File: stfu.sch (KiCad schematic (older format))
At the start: 136 parts, among them K1 FTDI, K2 ISP, K3 I2C, K4 SERVO, K5 V_SEL, P1 CONN_1, P2 CONN_1, Q1 PNP, SW1 RST, SW2 RST, SW3 SW_MODE, SW4 SW_INC, SW5 SW_DEC, SW6 SW_ENT, U1 ATMEGA328-P, U2 HEF4051B, U3 ULN2803, U4 7809, U5 7805, X1 16MHz

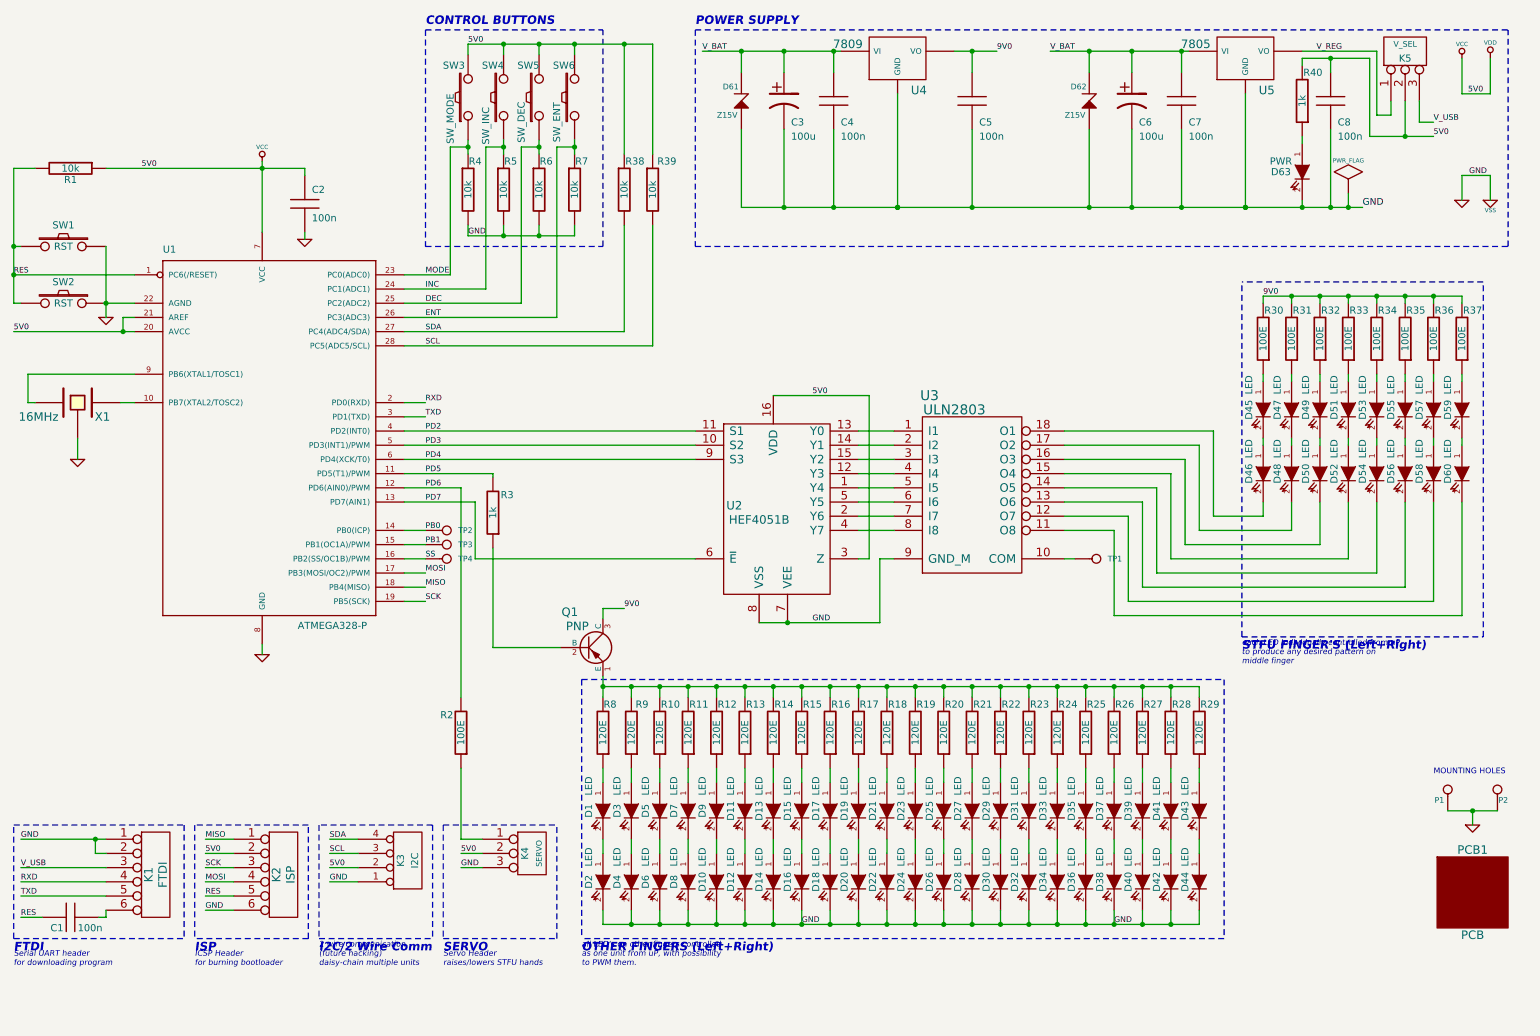
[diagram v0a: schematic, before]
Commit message: added the second Hand
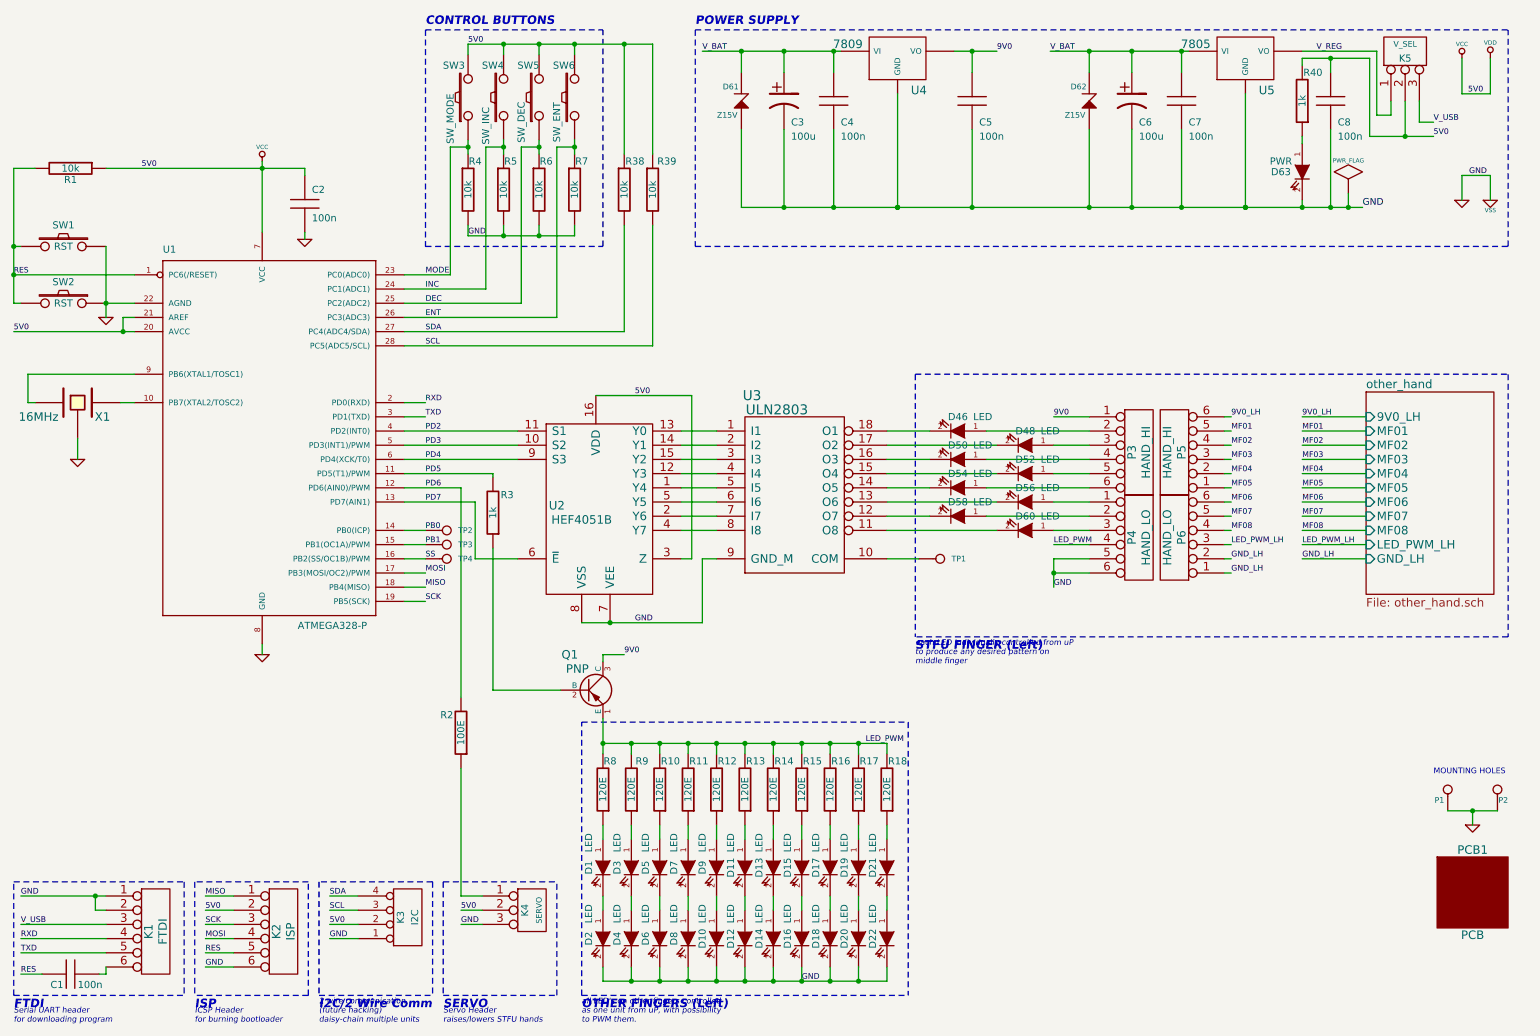
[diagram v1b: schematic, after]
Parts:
- removed D23, D24, D25, D26, D27, D28, D29, D30, D31, D32, D33, D34, D35, D36, D37, D38, D39, D40, D41, D42, D43, D44, D45, D47, D49, D51, D53, D55, D57, D59: LED, symbol LED
- removed R19, R20, R21, R22, R23, R24, R25, R26, R27, R28, R29: 120E, r_0805, symbol R
- removed R30, R31, R32, R33, R34, R35, R36, R37: 100E, r_0805, symbol R
- added P3, P5: HAND_HI, symbol CONN_6
- added P4, P6: HAND_LO, symbol CONN_6
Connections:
- net 9V0: now also P3.1
- net GND: now also P4.5, P4.6
- net LED_PWM: now reaches Q1.1 (E), R10.2, R11.2, R12.2, R13.2, R14.2, R15.2, R16.2, R17.2, R18.2, R8.2, R9.2
- net LED_PWM: now also P4.4
- net at D46.1 (A): now also P3.2
- net at D48.1 (A): now also P3.3
- net at D50.1 (A): now also P3.4
- net at D52.1 (A): now also P3.5
- net at D54.1 (A): now also P3.6
- net at D56.1 (A): now also P4.1
- net at D58.1 (A): now also P4.2
- net at D60.1 (A): now also P4.3
- new net 9V0_LH: P5.6
- new net GND_LH: P6.1, P6.2
- new net LED_PWM_LH: P6.3
- new net MF01: P5.5
- new net MF02: P5.4
- new net MF03: P5.3
- new net MF04: P5.2
- new net MF05: P5.1
- new net MF06: P6.6
- new net MF07: P6.5
- new net MF08: P6.4
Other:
- note added: "OTHER FINGERS (Left)"
- note added: "STFU FINGER (Left)"
- note removed: "OTHER FINGERS (Left+Right)"
- note removed: "STFU FINGER'S (Left+Right)"
- moved on the sheet: C1, D1, D10, D11, D12, D13, D14, D15, D16, D17, D18, D19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

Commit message: preliminary board layout
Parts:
- added P7: BATT_12V, symbol CONN_2
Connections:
- net GND: now also P7.1 (P1)
- net V_BAT: now also P7.2 (PM)
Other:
- moved on the sheet: C3, C4, C5, C6, D61, D62, U4
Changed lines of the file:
@@
-EESchema Schematic File Version 2  date 7/5/2012 5:41:43 PM
+EESchema Schematic File Version 2  date Monday 09 July 2012 12:59:22 AM IST
 LIBS:stfu
 LIBS:power
@@
 Sheet 1 2
 Title "STFU - a warning for incessant Noise polluters"
-Date "5 jul 2012"
+Date "8 jul 2012"
 Rev "A"
 Comp "anool.m@gmail.com"
@@
 $EndDescr
 Wire Notes Line
+	5600 2150 11125 2150
+Wire Notes Line
+	5600 2150 5600 625
+Wire Wire Line
+	6150 1375 6150 775
+Wire Wire Line
+	6150 1375 6100 1375
+Wire Notes Line
 	6950 3050 6950 4900
 Wire Notes Line
@@
 Wire Wire Line
 	6750 7325 4750 7325
-Connection ~ 8175 1875
-Wire Wire Line
-	8175 1875 8175 1325
+Connection ~ 8375 1875
+Wire Wire Line
+	8375 1875 8375 1325
 Wire Notes Line
 	3500 625  4750 625
@@
 Wire Notes Line
 	4750 2150 4750 625
-Wire Notes Line
-	5400 625  5400 2150
 Wire Wire Line
 	4900 5025 4750 5025
 Wire Wire Line
 	4750 5025 4750 5075
-Connection ~ 7350 775
-Wire Wire Line
-	7350 925  7350 775
-Connection ~ 5725 775
-Wire Wire Line
-	5725 925  5725 775
-Connection ~ 6825 1875
-Connection ~ 6375 775
-Connection ~ 6375 1875
-Wire Wire Line
-	6375 1875 6375 1325
-Connection ~ 6825 1875
-Wire Wire Line
-	6025 1325 6025 1875
-Wire Wire Line
-	6025 775  6025 925
-Wire Wire Line
-	6825 1875 6825 1075
-Wire Wire Line
-	6375 775  6375 925
-Connection ~ 6025 775
-Wire Wire Line
-	6425 775  5450 775
-Wire Wire Line
-	5725 1325 5725 1875
-Connection ~ 6025 1875
+Connection ~ 7750 775
+Wire Wire Line
+	7750 925  7750 775
+Connection ~ 6325 775
+Wire Wire Line
+	6325 775  6325 925
+Connection ~ 7275 1875
+Connection ~ 6775 775
+Connection ~ 6775 1875
+Wire Wire Line
+	6775 1875 6775 1325
+Connection ~ 7275 1875
+Wire Wire Line
+	6525 1875 6525 1325
+Wire Wire Line
+	6525 775  6525 925
+Wire Wire Line
+	7275 1875 7275 1075
+Wire Wire Line
+	6775 925  6775 775
+Connection ~ 6525 775
+Wire Wire Line
+	6150 775  6875 775
+Wire Wire Line
+	6325 1325 6325 1875
+Connection ~ 6525 1875
 Wire Wire Line
 	6750 4150 7525 4150
@@
 Wire Wire Line
 	650  2150 600  2150
-Connection ~ 8475 1875
-Wire Wire Line
-	5725 1875 10100 1875
+Connection ~ 8575 1875
 Connection ~ 10875 6125
 Wire Wire Line
@@
 	1950 7125 2150 7125
 Wire Wire Line
-	8875 775  7900 775
-Connection ~ 8475 775
+	8875 775  8175 775
+Connection ~ 8575 775
 Connection ~ 9875 825
 Wire Wire Line
 	9875 925  9875 825
 Wire Wire Line
-	8825 925  8825 775
+	8825 775  8825 925
 Wire Wire Line
 	9675 1875 9675 1825
@@
 	9275 1875 9275 1075
 Wire Wire Line
-	8475 775  8475 925
+	8575 775  8575 925
 Connection ~ 9675 1875
 Wire Wire Line
-	8475 1875 8475 1325
+	8575 1875 8575 1325
 Connection ~ 9275 1875
 Wire Wire Line
@@
 Connection ~ 9875 1875
 Wire Wire Line
-	10000 1775 10000 1875
+	10000 1875 10000 1775
 Connection ~ 10000 1875
 Wire Wire Line
-	8175 775  8175 925
-Connection ~ 8175 775
+	8375 925  8375 775
+Connection ~ 8375 775
 Wire Wire Line
 	1250 2150 1250 2650
@@
 	7050 4050 6750 4050
 Wire Wire Line
-	7525 775  7225 775
-Wire Wire Line
-	7350 1875 7350 1325
-Connection ~ 7350 1875
-Wire Notes Line
-	5400 625  11125 625
-Wire Notes Line
-	5400 2150 11125 2150
+	7800 775  7675 775
+Wire Wire Line
+	7750 1875 7750 1325
+Connection ~ 7750 1875
 Wire Notes Line
 	11125 2150 11125 625
@@
 Wire Notes Line
 	11125 4900 6950 4900
+Wire Wire Line
+	6100 1575 6150 1575
+Wire Wire Line
+	6150 1575 6150 1875
+Wire Wire Line
+	6150 1875 10100 1875
+Connection ~ 6325 1875
+Wire Notes Line
+	11125 625  5600 625
+$Comp
+L CONN_2 P7
+U 1 1 4FF99A4C
+P 5750 1475
+F 0 "P7" V 5700 1475 40  0000 C CNN
+F 1 "BATT_12V" V 5800 1475 40  0000 C CNN
+	1    5750 1475
+	-1   0    0    1
+$EndComp
 Text Label 9675 3350 0    40   ~ 0
 9V0_LH
@@
 L C C5
 U 1 1 4FF2E982
-P 7350 1125
-F 0 "C5" H 7400 975 50  0000 L CNN
-F 1 "100n" H 7400 875 50  0000 L CNN
-F 2 "C2" H 7350 1125 60  0001 C CNN
-	1    7350 1125
-	1    0    0    -1
-$EndComp
-Text Label 7525 775  0    40   ~ 0
+P 7750 1125
+F 0 "C5" H 7800 975 50  0000 L CNN
+F 1 "100n" H 7800 875 50  0000 L CNN
+F 2 "C2" H 7750 1125 60  0001 C CNN
+	1    7750 1125
+	1    0    0    -1
+$EndComp
+Text Label 7800 775  0    40   ~ 0
 9V0
 $Comp
 L DIODE_ZENER D61
 U 1 1 4FF2E927
-P 5725 1125
-F 0 "D61" V 5825 1200 40  0000 C CNN
-F 1 "Z15V" V 5625 1225 40  0000 C CNN
-F 2 "DO-35_Vert" H 5725 1125 60  0001 C CNN
-	1    5725 1125
+P 6325 1125
+F 0 "D61" V 6425 1200 40  0000 C CNN
+F 1 "Z15V" V 6225 1225 40  0000 C CNN
+F 2 "DO-35_Vert" H 6325 1125 60  0001 C CNN
+	1    6325 1125
 	0    -1   -1   0
 $EndComp
@@
 L CP1 C3
 U 1 1 4FF2E926
-P 6025 1125
-F 0 "C3" H 6075 975 50  0000 L CNN
-F 1 "100u" H 6075 875 50  0000 L CNN
-F 2 "CP_5x11mm" H 6025 1125 60  0001 C CNN
-	1    6025 1125
+P 6525 1125
+F 0 "C3" H 6575 975 50  0000 L CNN
+F 1 "100u" H 6575 875 50  0000 L CNN
+F 2 "CP_5x11mm" H 6525 1125 60  0001 C CNN
+	1    6525 1125
 	1    0    0    -1
 $EndComp
@@
 L C C4
 U 1 1 4FF2E925
-P 6375 1125
-F 0 "C4" H 6425 975 50  0000 L CNN
-F 1 "100n" H 6425 875 50  0000 L CNN
-F 2 "C2" H 6375 1125 60  0001 C CNN
-	1    6375 1125
-	1    0    0    -1
-$EndComp
-Text Label 5450 775  0    40   ~ 0
+P 6775 1125
+F 0 "C4" H 6825 975 50  0000 L CNN
+F 1 "100n" H 6825 875 50  0000 L CNN
+F 2 "C2" H 6775 1125 60  0001 C CNN
+	1    6775 1125
+	1    0    0    -1
+$EndComp
+Text Label 6175 775  0    40   ~ 0
 V_BAT
 $Comp
 L 7805 U4
 U 1 1 4FF2E924
-P 6825 825
-F 0 "U4" H 6975 600 60  0000 C CNN
-F 1 "7809" H 6475 925 60  0000 C CNN
-F 2 "TO-220_Vertical" H 6825 825 60  0001 C CNN
-	1    6825 825
+P 7275 825
+F 0 "U4" H 7425 600 60  0000 C CNN
+F 1 "7809" H 6925 925 60  0000 C CNN
+F 2 "TO-220_Vertical" H 7275 825 60  0001 C CNN
+	1    7275 825
 	1    0    0    -1
 $EndComp
@@
 $EndComp
 $Comp
-L GND #PWR01
+L GND #PWR1
 U 1 1 4FF29B8E
 P 1050 3650
-F 0 "#PWR01" H 1050 3650 30  0001 C CNN
+F 0 "#PWR1" H 1050 3650 30  0001 C CNN
 F 1 "GND" H 1050 3580 30  0001 C CNN
 	1    1050 3650
@@
 $EndComp
 $Comp
-L GND #PWR02
+L GND #PWR2
 U 1 1 4FF29B8D
 P 1250 2650
-F 0 "#PWR02" H 1250 2650 30  0001 C CNN
+F 0 "#PWR2" H 1250 2650 30  0001 C CNN
 F 1 "GND" H 1250 2580 30  0001 C CNN
 	1    1250 2650
@@
 $EndComp
 $Comp
-L VCC #PWR03
+L VCC #PWR3
 U 1 1 4FF29B8C
 P 2350 1550
-F 0 "#PWR03" H 2350 1650 30  0001 C CNN
+F 0 "#PWR3" H 2350 1650 30  0001 C CNN
 F 1 "VCC" H 2350 1650 30  0000 C CNN
 	1    2350 1550
@@
 $EndComp
 $Comp
-L GND #PWR04
+L GND #PWR4
 U 1 1 4FF29B8B
 P 2350 5025
-F 0 "#PWR04" H 2350 5025 30  0001 C CNN
+F 0 "#PWR4" H 2350 5025 30  0001 C CNN
 F 1 "GND" H 2350 4955 30  0001 C CNN
 	1    2350 5025
@@
 $EndComp
 $Comp
-L GND #PWR05
+L GND #PWR5
 U 1 1 4FF29B88
 P 2650 2100
-F 0 "#PWR05" H 2650 2100 30  0001 C CNN
+F 0 "#PWR5" H 2650 2100 30  0001 C CNN
 F 1 "GND" H 2650 2030 30  0001 C CNN
 	1    2650 2100
@@
 $EndComp
 $Comp
-L VCC #PWR06
+L VCC #PWR6
 U 1 1 4FF29B70
 P 10800 825
-F 0 "#PWR06" H 10800 925 30  0001 C CNN
+F 0 "#PWR6" H 10800 925 30  0001 C CNN
 F 1 "VCC" H 10800 925 30  0000 C CNN
 	1    10800 825
@@
 $EndComp
 $Comp
-L GND #PWR07
+L GND #PWR7
 U 1 1 4FF29B6F
 P 10800 1825
-F 0 "#PWR07" H 10800 1825 30  0001 C CNN
+F 0 "#PWR7" H 10800 1825 30  0001 C CNN
 F 1 "GND" H 10800 1755 30  0001 C CNN
 	1    10800 1825
@@
 $EndComp
 $Comp
-L VDD #PWR08
+L VDD #PWR9
 U 1 1 4FF29B6D
 P 11000 825
-F 0 "#PWR08" H 11000 925 30  0001 C CNN
+F 0 "#PWR9" H 11000 925 30  0001 C CNN
 F 1 "VDD" H 11000 935 30  0000 C CNN
 	1    11000 825
@@
 RES
 $Comp
-L VSS #PWR09
+L VSS #PWR10
 U 1 1 4FF29B6B
 P 11000 1825
-F 0 "#PWR09" H 11000 1825 30  0001 C CNN
+F 0 "#PWR10" H 11000 1825 30  0001 C CNN
 F 1 "VSS" H 11000 1755 30  0000 C CNN
 	1    11000 1825
@@
 ISP
 $Comp
-L PWR_FLAG #FLG010
+L PWR_FLAG #FLG1
 U 1 1 4FF29B6A
 P 10000 1775
-F 0 "#FLG010" H 10000 2045 30  0001 C CNN
+F 0 "#FLG1" H 10000 2045 30  0001 C CNN
 F 1 "PWR_FLAG" H 10000 2005 30  0000 C CNN
 	1    10000 1775
@@
 	1    0    0    -1
 $EndComp
-Text Label 7900 775  0    40   ~ 0
+Text Label 8175 775  0    40   ~ 0
 V_BAT
 Text Label 10600 1375 0    40   ~ 0
@@
 L CP1 C6
 U 1 1 4FF29B62
-P 8475 1125
-F 0 "C6" H 8525 975 50  0000 L CNN
-F 1 "100u" H 8525 875 50  0000 L CNN
-F 2 "CP_5x11mm" H 8475 1125 60  0001 C CNN
-	1    8475 1125
-	1    0    0    -1
-$EndComp
-Text Notes 5400 600  0    60   Italic 12
+P 8575 1125
+F 0 "C6" H 8625 975 50  0000 L CNN
+F 1 "100u" H 8625 875 50  0000 L CNN
+F 2 "CP_5x11mm" H 8575 1125 60  0001 C CNN
+	1    8575 1125
+	1    0    0    -1
+$EndComp
+Text Notes 5600 600  0    60   Italic 12
 POWER SUPPLY
 Text Label 3500 2550 0    40   ~ 0
@@
 MOUNTING HOLES
 $Comp
-L GND #PWR011
+L GND #PWR8
 U 1 1 4FF29B54
 P 10875 6225
-F 0 "#PWR011" H 10875 6225 30  0001 C CNN
+F 0 "#PWR8" H 10875 6225 30  0001 C CNN
 F 1 "GND" H 10875 6155 30  0001 C CNN
 	1    10875 6225
@@
 L DIODE_ZENER D62
 U 1 1 4FF29B4B
-P 8175 1125
-F 0 "D62" V 8275 1200 40  0000 C CNN
-F 1 "Z15V" V 8075 1225 40  0000 C CNN
-F 2 "DO-35_Vert" H 8175 1125 60  0001 C CNN
-	1    8175 1125
+P 8375 1125
+F 0 "D62" V 8475 1200 40  0000 C CNN
+F 1 "Z15V" V 8275 1225 40  0000 C CNN
+F 2 "DO-35_Vert" H 8375 1125 60  0001 C CNN
+	1    8375 1125
 	0    -1   -1   0
 $EndComp
